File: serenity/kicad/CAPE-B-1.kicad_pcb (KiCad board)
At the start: 4 copper layers, 55 x 35 mm, 33 parts, among them J1 PB2I-P1-2x18, J10 Nano-Fit-4P-POWER, J11 JST-GH-4P-WINCH, J12 JST-GH-4P-LOAD-CELL, J13 1x8-NavLight-PWM, J2 PB2I-P2-2x18, J3 JST-GH-4P-CAN, J4 JST-GH-4P-RS485, J5 JST-GH-4P-1553, J6 JST-GH-6P-ETH1, J7 JST-GH-6P-ETH2, J8 JST-GH-3P-SiK, J9 JST-GH-3P-RCRS, T1 SM-1553-11, U1 RFM95W, U10 ATF16V8BQL, U11 W25Q128JV, U12 DRV8833, U13 HX711, U14 PCA9685, U2 WL1837MOD, U3 ATA6561, U4 MAX3485E, U5 DS26LV31, U6 DS26LV32, U7 DP83825I, U8 DP83825I, U9 SLB9670

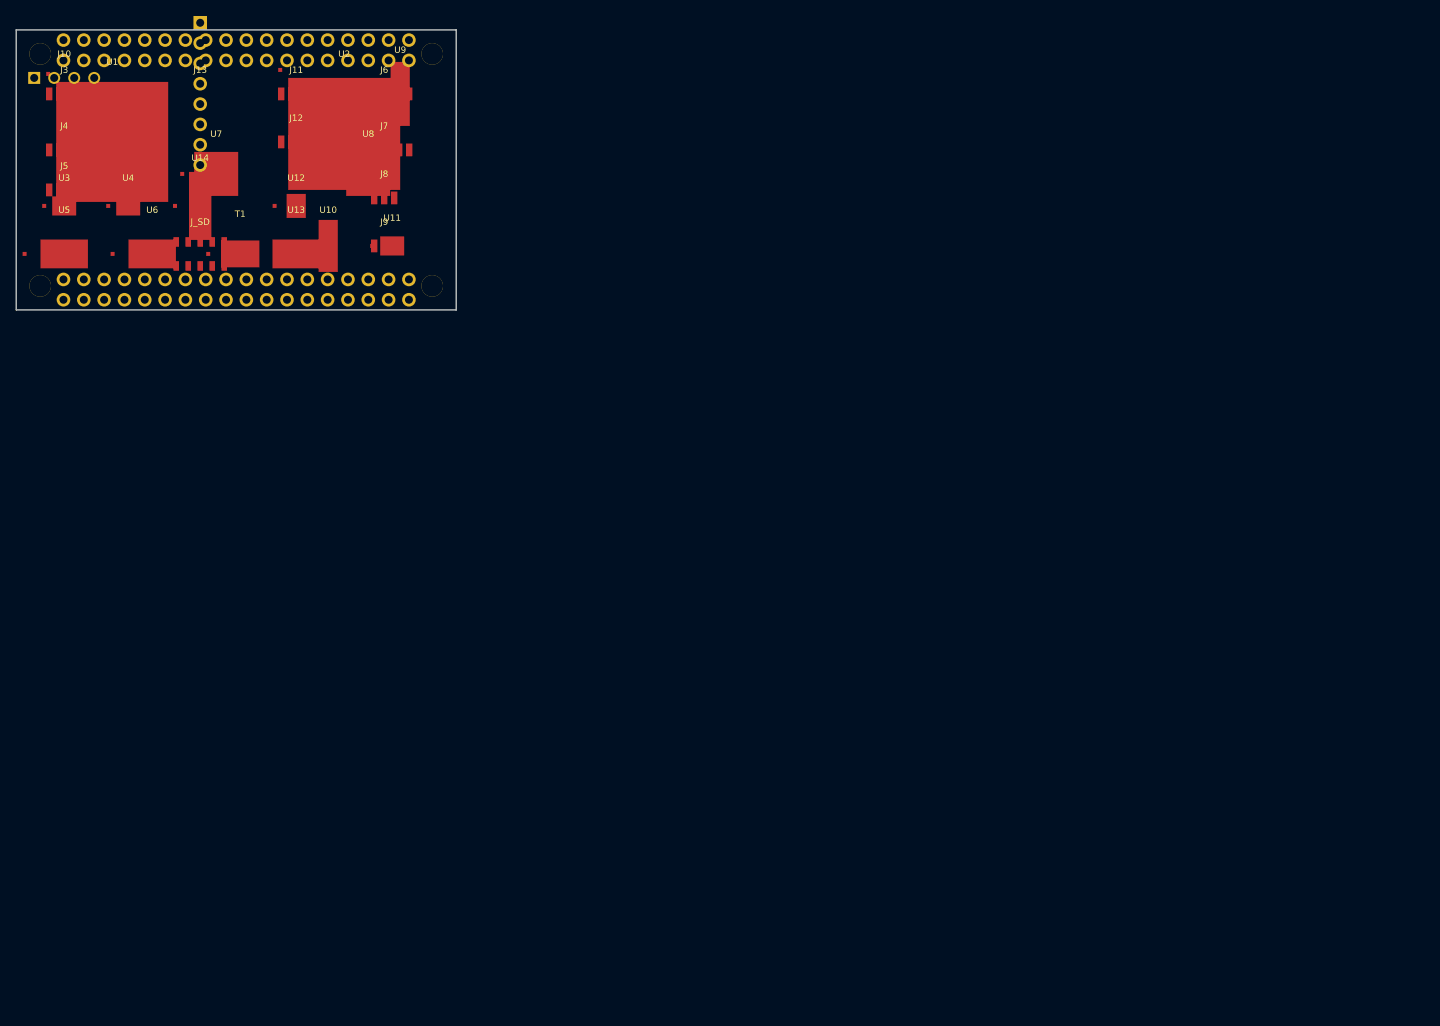
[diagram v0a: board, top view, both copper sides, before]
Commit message: Rev M: populate CAPE-A/B schematics and center PCBs on A4 drawing page
- CAPE-A-1.kicad_sch: full schematic with Conn_36 J1/J2 expansion headers
  (36 pins each, all nets labeled), ICM-42688-P, BMP388, SAM-M10Q, ATA6561,
  MAX3485E, DS26LV31/32, SM-1553-11, DP83825I×2, SLB9670; 142 global labels
  connecting expansion header nets to IC pins
- CAPE-B-1.kicad_sch: full schematic with RFM95W, WL1837MOD, ATA6561,
  MAX3485E, DS26LV31/32, SM-1553-11, DP83825I×2, SLB9670, ATF16V8BQL,
  W25Q128JV, DRV8833, HX711, PCA9685, microSD; 169 global labels
- CAPE-A-1.kicad_pcb, CAPE-B-1.kicad_pcb: board outline shifted from
  origin (0,0)–(55,35) to (121,87.5)–(176,122.5), centering 55×35mm board
  on A4 (297×210mm) drawing sheet; footprint absolute positions updated,
  inner relative pad/courtyard coordinates unchanged

Co-Authored-By: Claude Sonnet 4.6 <noreply@anthropic.com>
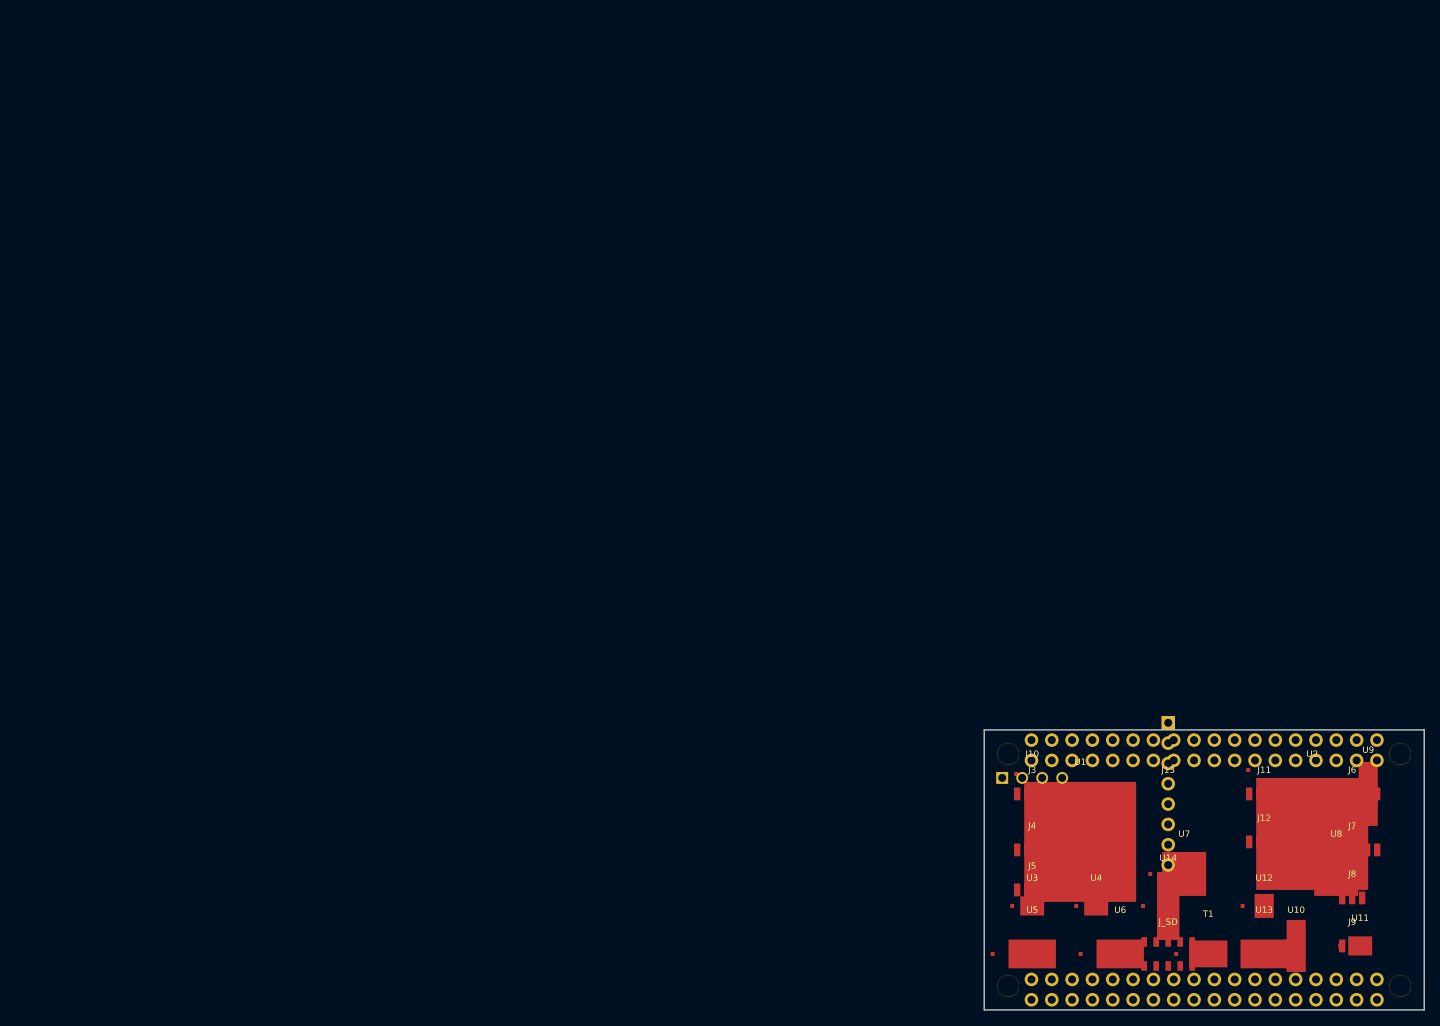
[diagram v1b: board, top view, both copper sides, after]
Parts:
- removed the ? at (3.00, 3.00)
- removed the ? at (52.0, 3.00)
- removed the ? at (3.00, 32.0)
- removed the ? at (52.0, 32.0)
- added ?: , MountingHole:MountingHole_2.7mm_M2.5, F.Cu at (124.0, 90.5)
- added ?: , MountingHole:MountingHole_2.7mm_M2.5, F.Cu at (173.0, 90.5)
- added ?: , MountingHole:MountingHole_2.7mm_M2.5, F.Cu at (124.0, 119.5)
- added ?: , MountingHole:MountingHole_2.7mm_M2.5, F.Cu at (173.0, 119.5)
- moved J1 149.3 mm to (148.5, 90.0)
- moved J10 149.3 mm to (127.0, 93.5)
- moved J11 149.3 mm to (156.0, 95.5)
- moved J12 149.3 mm to (156.0, 101.5)
- moved J13 149.3 mm to (144.0, 95.5)
- moved J2 149.3 mm to (148.5, 120.0)
- moved J3 149.3 mm to (127.0, 95.5)
- moved J4 149.3 mm to (127.0, 102.5)
- moved J5 149.3 mm to (127.0, 107.5)
- moved J6 149.3 mm to (167.0, 95.5)
- moved J7 149.3 mm to (167.0, 102.5)
- moved J8 149.3 mm to (167.0, 108.5)
- moved J9 149.3 mm to (167.0, 114.5)
- moved J_SD 149.3 mm to (144.0, 115.5)
- moved T1 149.3 mm to (149.0, 115.5)
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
